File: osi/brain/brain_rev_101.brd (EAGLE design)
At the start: 25.4 x 25.4 mm, 4 parts

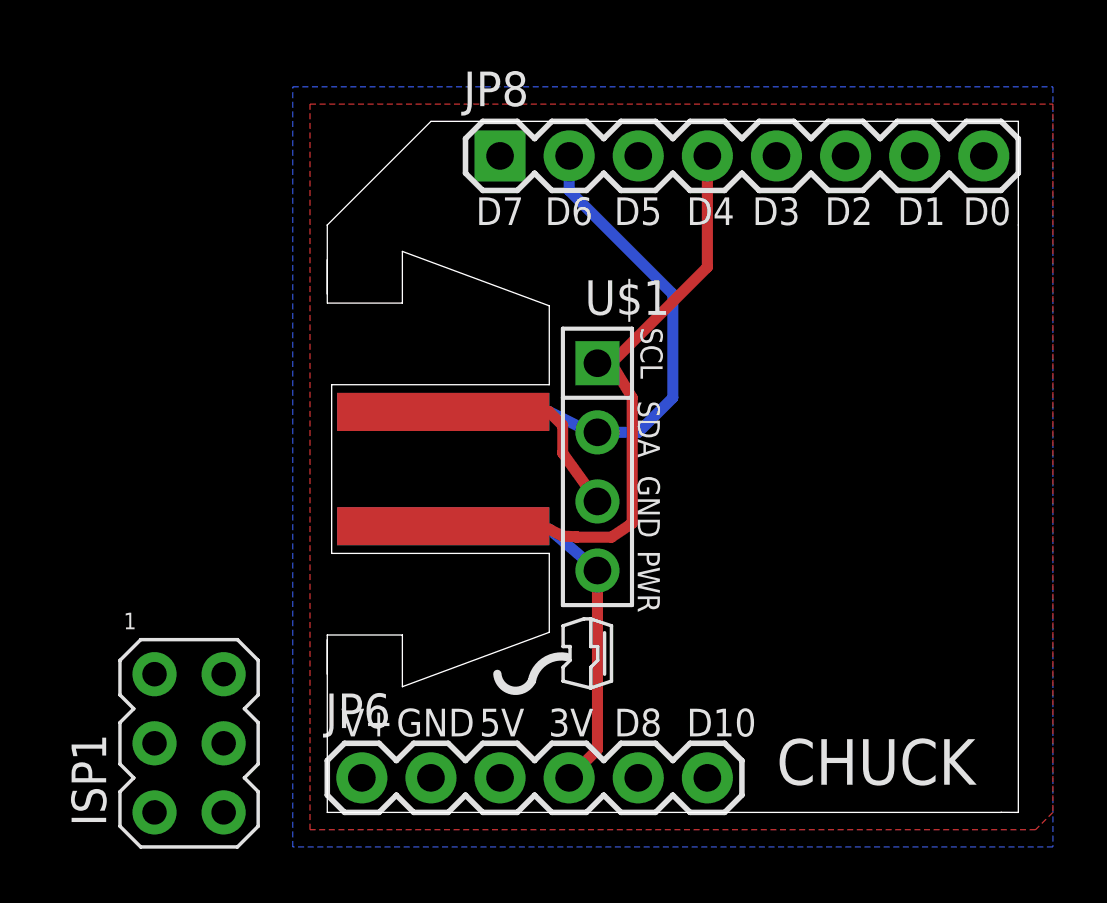
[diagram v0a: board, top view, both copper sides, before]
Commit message: Moving RST line in brain
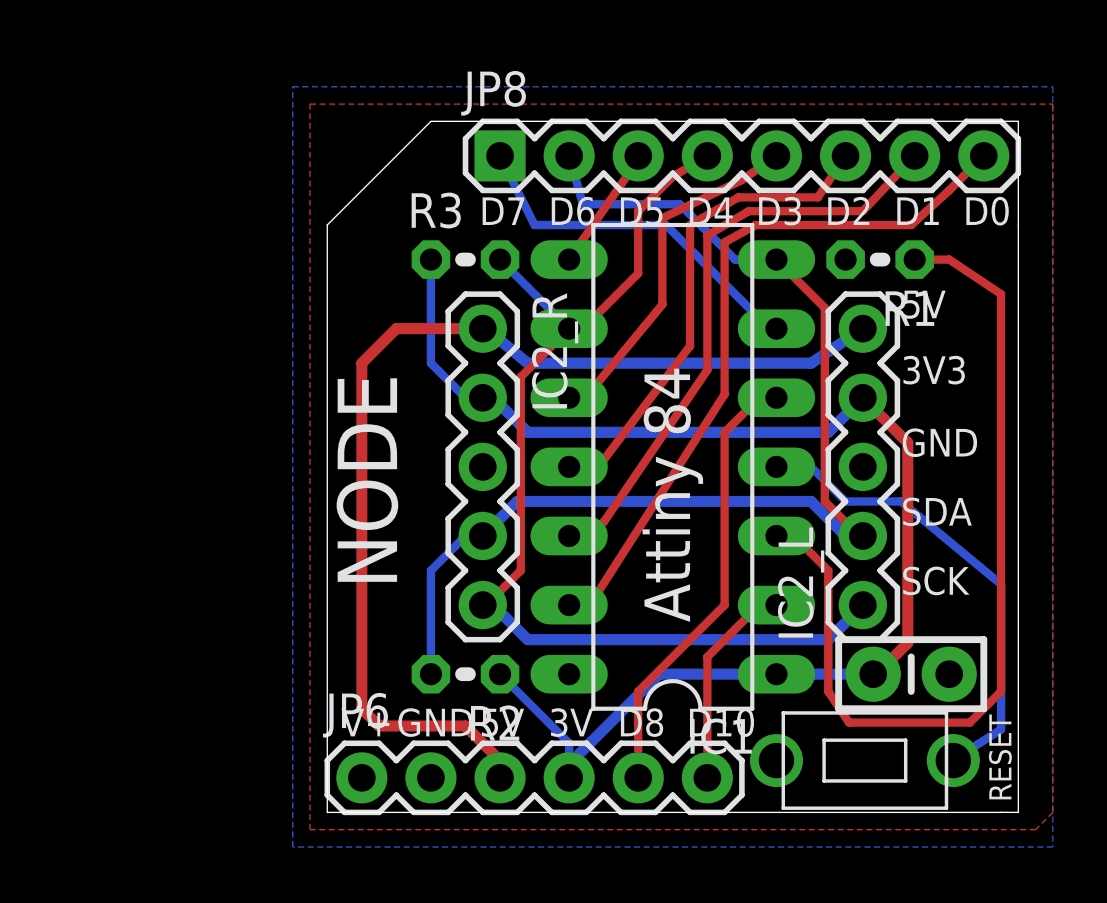
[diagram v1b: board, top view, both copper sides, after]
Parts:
- removed ISP1: AVRISP-6, adafruit_mod:AVRISP
- added C1: (no value), SparkFun:CAP-PTH-SMALL-KIT
- added IC1: TINY24/44/84-PU, avr-7:DIL14
- added IC2_L, IC2_R: (no value), SparkFun_mod:1X05
- added R1, R2, R3: (no value), adafruit_mod:0204V
- U$1: value NUNCHUCKCHUCK -> PTS635_SWITCH; device _my-parts:CONN -> _my-parts:PTS635_SWITCH
- moved U$1 8.54 mm to (16.5, 1.91)
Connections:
- new net D1: IC1.12, JP8.7
- new net D9: IC1.3, R1.1
- new net RESET: IC1.4, U$1.P$2
- net +3V3: now also C1.2, IC1.1, IC2_L.4, IC2_R.2, R2.1, R3.1; no longer ISP1.2, U$1.VCC
- net +5V: now also IC2_L.5, IC2_R.1
- net AREF_D0: now also IC1.13
- net D10: now also IC1.2
- net D2: now also IC1.11
- net D3: now also IC1.10
- net D5: now also IC1.8; no longer ISP1.1
- net D7: now also IC1.6
- net D8: now also IC1.5
- net GND: now also C1.1, IC1.14, IC2_L.3, IC2_R.3, R1.2, U$1.P$1; no longer ISP1.6, U$1.GND
- net SCL_D4: now also IC1.9, IC2_L.1, IC2_R.5, R3.2; no longer U$1.SCL
- net SDA_D6: now also IC1.7, IC2_L.2, IC2_R.4, R2.2; no longer ISP1.4, U$1.SDA
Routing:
- net +3V3: track 8.05 -> 50.5 mm
- net +5V: track 0.00 -> 39.0 mm
- net D9: track 0.00 -> 32.5 mm
- net SCL_D4: track 9.08 -> 39.1 mm
- net SDA_D6: track 13.8 -> 42.6 mm
- net AREF_D0: track 0.00 -> 26.3 mm
- net D1: track 0.00 -> 21.9 mm
- net D2: track 0.00 -> 17.9 mm
- net RESET: track 0.00 -> 17.3 mm
- net D8: track 0.00 -> 16.4 mm
- net D7: track 0.00 -> 13.3 mm
- net D3: track 0.00 -> 13.0 mm
- net D10: track 0.00 -> 7.77 mm
- net D5: track 0.00 -> 4.58 mm
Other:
- outline, holes or cut-outs redrawn
- board text added: "3V3"
- board text added: "Attiny 84"
- board text added: "NODE"
- board text added: "RESET"
- board text added: "Rev 1 Mar 12"
- board text added: "SCK"
- board text added: "SDA"
- board text removed: "CHUCK"
- board text removed: "CHUCK Rev 1 Feb 12"

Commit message: continue on brain
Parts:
- moved R1 22.5 mm to (5.08, 3.81)
- moved R3 2.84 mm to (3.81, 22.9)
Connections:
- removed net D10: IC1.2, JP6.6
- net RESET: now also JP6.6
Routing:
- net D9: track 32.5 -> 0.00 mm
- net D10: track 7.77 -> 0.00 mm
- net +3V3: track 50.5 -> 44.9 mm
- net SCL_D4: track 39.1 -> 35.5 mm
- net +5V: track 39.0 -> 36.4 mm
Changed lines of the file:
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@@
 <element name="JP6" library="SparkFun" package="1X06" value="" x="1.27" y="1.27"/>
 <element name="JP8" library="SparkFun" package="1X08" value="" x="6.35" y="24.13"/>
-<element name="R1" library="adafruit_mod" package="0204V" value="" x="20.32" y="20.32" rot="R180"/>
+<element name="R1" library="adafruit_mod" package="0204V" value="" x="5.08" y="3.81" rot="R180"/>
 <element name="R2" library="adafruit_mod" package="0204V" value="" x="5.08" y="5.08" rot="R180"/>
-<element name="R3" library="adafruit_mod" package="0204V" value="" x="5.08" y="20.32"/>
+<element name="R3" library="adafruit_mod" package="0204V" value="" x="3.81" y="22.86"/>
 </elements>
 <signals>
@@
 <wire x1="24.765" y1="3.048" x2="23.01" y2="1.928" width="0.3048" layer="16"/>
 <wire x1="23.01" y1="1.928" x2="23.01" y2="1.905" width="0.3048" layer="16"/>
+<contactref element="JP6" pad="6"/>
+<wire x1="13.97" y1="1.27" x2="23.01" y2="1.905" width="0" layer="19" extent="1-1"/>
 </signal>
 <signal name="D3">
@@
 <wire x1="5.842" y1="7.62" x2="5.715" y2="7.62" width="0.3048" layer="1"/>
 <contactref element="R3" pad="2"/>
-<wire x1="6.35" y1="20.32" x2="8.89" y2="17.78" width="0.3048" layer="16"/>
+<wire x1="5.08" y1="22.86" x2="8.89" y2="17.78" width="0" layer="19" extent="1-16"/>
 </signal>
 <signal name="D9">
 <contactref element="IC1" pad="3"/>
 <contactref element="R1" pad="1"/>
-<wire x1="16.51" y1="10.16" x2="17.145" y2="10.16" width="0.3048" layer="1"/>
-<wire x1="17.145" y1="10.16" x2="18.415" y2="8.89" width="0.3048" layer="1"/>
-<wire x1="18.415" y1="8.89" x2="18.415" y2="4.445" width="0.3048" layer="1"/>
-<wire x1="18.415" y1="4.445" x2="19.177" y2="3.302" width="0.3048" layer="1"/>
-<wire x1="19.177" y1="3.302" x2="23.622" y2="3.302" width="0.3048" layer="1"/>
-<wire x1="23.622" y1="3.302" x2="24.765" y2="4.445" width="0.3048" layer="1"/>
-<wire x1="24.765" y1="4.445" x2="24.765" y2="19.05" width="0.3048" layer="1"/>
-<wire x1="24.765" y1="19.05" x2="22.86" y2="20.32" width="0.3048" layer="1"/>
-<wire x1="22.86" y1="20.32" x2="21.59" y2="20.32" width="0.3048" layer="1"/>
-</signal>
-<signal name="D10">
-<contactref element="IC1" pad="2"/>
-<contactref element="JP6" pad="6"/>
-<wire x1="16.51" y1="7.62" x2="15.875" y2="7.62" width="0.3048" layer="1"/>
-<wire x1="15.875" y1="7.62" x2="13.97" y2="5.715" width="0.3048" layer="1"/>
-<wire x1="13.97" y1="5.715" x2="13.97" y2="1.27" width="0.3048" layer="1"/>
+<wire x1="16.51" y1="10.16" x2="6.35" y2="3.81" width="0" layer="19" extent="1-1"/>
 </signal>
 <signal name="D7">
@@
 <contactref element="R2" pad="1"/>
 <wire x1="5.715" y1="15.24" x2="5.08" y2="15.24" width="0.3048" layer="16"/>
-<wire x1="5.08" y1="15.24" x2="3.81" y2="16.51" width="0.3048" layer="16"/>
-<wire x1="3.81" y1="16.51" x2="3.81" y2="20.32" width="0.3048" layer="16"/>
+<wire x1="5.08" y1="15.24" x2="3.81" y2="16.51" width="0" layer="19" extent="1-16"/>
+<wire x1="3.81" y1="16.51" x2="2.54" y2="22.86" width="0" layer="19" extent="1-16"/>
 <wire x1="8.89" y1="1.778" x2="8.89" y2="2.54" width="0.3048" layer="16"/>
 <wire x1="8.89" y1="2.54" x2="6.35" y2="5.08" width="0.3048" layer="16"/>
@@
 <contactref element="IC2_L" pad="5"/>
 <contactref element="IC2_R" pad="1"/>
-<wire x1="5.08" y1="3.175" x2="1.905" y2="3.175" width="0.4064" layer="1"/>
-<wire x1="1.905" y1="3.175" x2="1.27" y2="3.81" width="0.4064" layer="1"/>
-<wire x1="1.27" y1="3.81" x2="1.27" y2="16.51" width="0.4064" layer="1"/>
-<wire x1="1.27" y1="16.51" x2="2.54" y2="17.78" width="0.4064" layer="1"/>
-<wire x1="2.54" y1="17.78" x2="5.715" y2="17.78" width="0.4064" layer="1"/>
+<wire x1="5.08" y1="3.175" x2="3.175" y2="3.175" width="0.4064" layer="1"/>
+<wire x1="3.175" y1="3.175" x2="2.54" y2="3.81" width="0.4064" layer="1"/>
+<wire x1="2.54" y1="3.81" x2="2.54" y2="16.51" width="0.4064" layer="1"/>
+<wire x1="2.54" y1="16.51" x2="3.81" y2="17.78" width="0.4064" layer="1"/>
+<wire x1="3.81" y1="17.78" x2="5.715" y2="17.78" width="0.4064" layer="1"/>
 <contactref element="JP6" pad="3"/>
 <wire x1="6.35" y1="1.27" x2="6.35" y2="1.905" width="0.4064" layer="1"/>

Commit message: Programming shield ver 1.2
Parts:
- removed IC2_L, IC2_R: (no value), SparkFun_mod:1X05
- removed JP8: (no value), SparkFun:1X08
- added J1: AVR_SPI_PRG_6PTH, SparkFun_mod:2X3
- added JP1, JP2: (no value), SparkFun_mod:1X04
- added JP3, JP4: (no value), SparkFun_mod:1X02
- added JP5: (no value), SparkFun_mod:1X08
- moved R1 2.44 mm to (2.67, 3.43)
- moved R2 2.43 mm to (2.67, 5.33)
- moved R3 0.38 mm to (3.81, 22.5)
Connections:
- net +3V3: now also JP1.1, JP2.4; no longer IC2_L.4, IC2_R.2
- net +5V: now also JP3.2, JP4.1; no longer IC2_L.5, IC2_R.1
- net AREF_D0: now also JP5.8; no longer JP8.8
- net D1: now also JP5.7; no longer JP8.7
- net D2: now also JP5.6; no longer JP8.6
- net D3: now also JP5.5; no longer JP8.5
- net D5: now also JP5.3; no longer JP8.3
- net D7: now also JP5.1; no longer JP8.1
- net GND: now also JP1.2, JP2.3; no longer IC2_L.3, IC2_R.3
- net SCL_D4: now also JP1.4, JP2.1, JP5.4; no longer IC2_L.1, IC2_R.5, JP8.4
- net SDA_D6: now also JP1.3, JP2.2, JP5.2; no longer IC2_L.2, IC2_R.4, JP8.2
- net V+: now also JP3.1, JP4.2
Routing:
- net SDA_D6: track 42.6 -> 19.4 mm
- net SCL_D4: track 35.5 -> 18.6 mm
- net +5V: track 36.4 -> 20.5 mm
- net +3V3: track 44.9 -> 29.0 mm
